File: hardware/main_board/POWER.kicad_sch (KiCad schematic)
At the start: 1 part, among them J1 USB_C_Receptacle_PowerOnly_6P

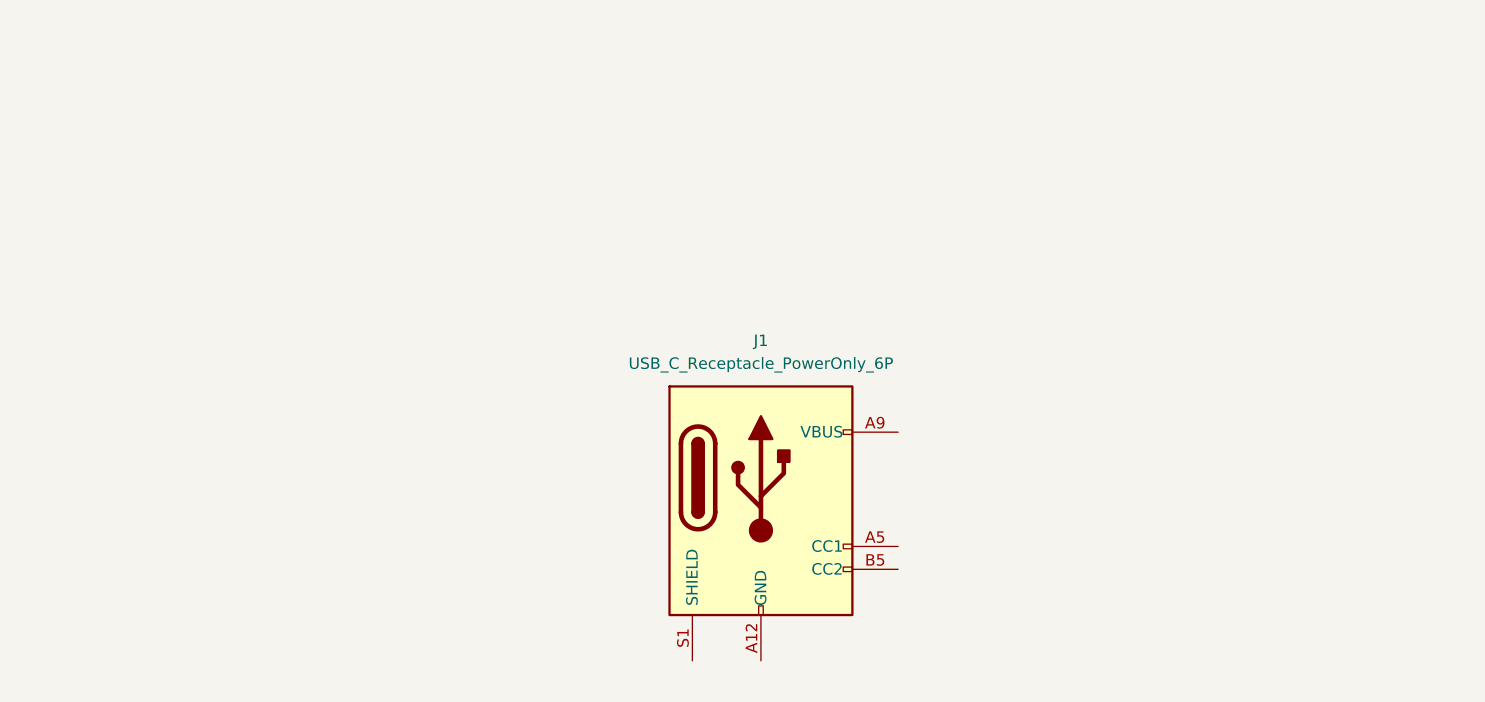
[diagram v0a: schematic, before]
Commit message: fixed sides of peripheral board not being symmetrical. added teardrops. name of board tbd
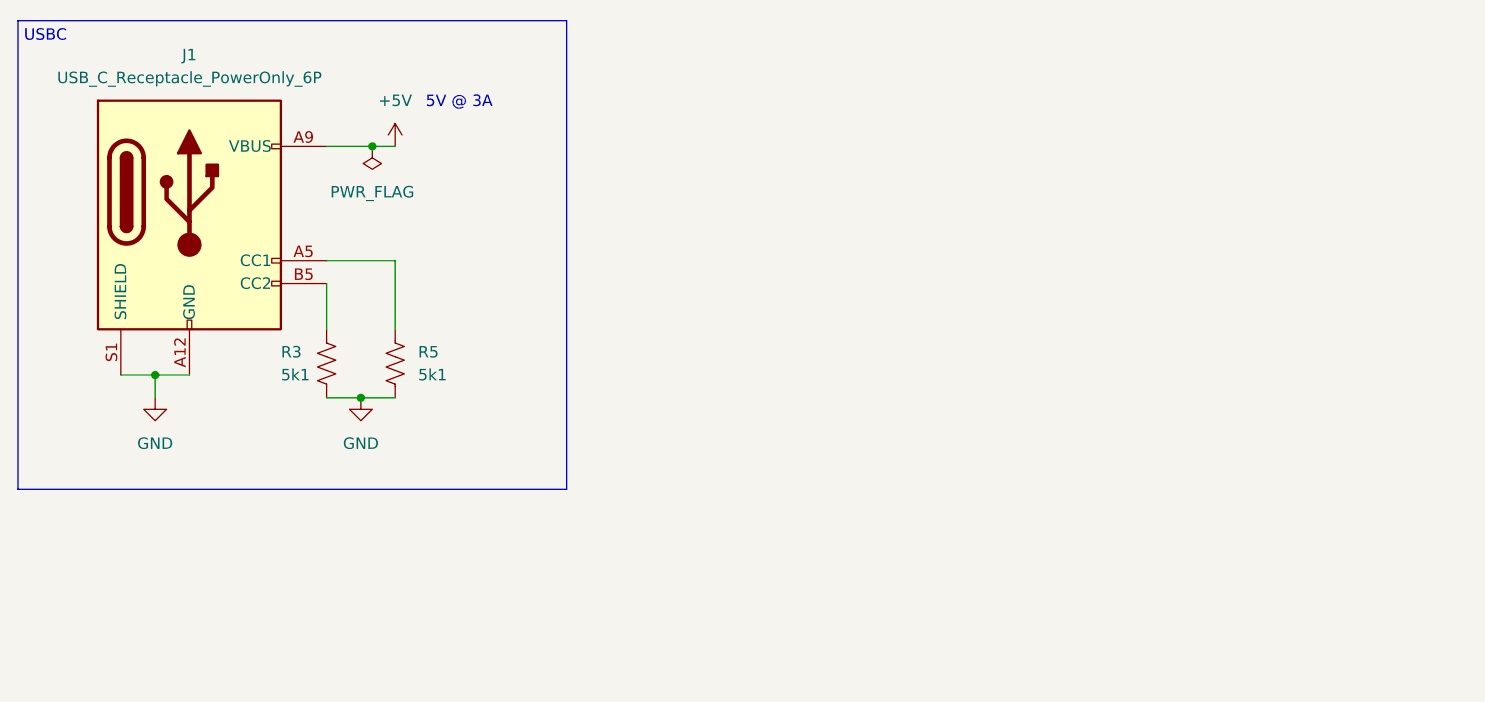
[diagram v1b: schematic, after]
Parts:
- added R3, R5: 5k1, symbol Device:R_US
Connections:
- net GND: now reaches J1.A12 (GND), J1.B12 (GND)
- net GND: now also J1.S1 (SHIELD), R3.2, R5.2
- net at J1.A5 (CC1): now also R5.1
- net +5V: now reaches J1.A9 (VBUS), J1.B9 (VBUS)
- net at J1.B5 (CC2): now also R3.1
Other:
- note added: "5V @ 3A"
- note added: "USBC"
- moved on the sheet: J1

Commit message: drew schematic
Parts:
- removed J1: USB_C_Receptacle_PowerOnly_6P, symbol Connector:USB_C_Receptacle_PowerOnly_6P
- added C10, C11, C9: 10u, Capacitor_SMD:C_0805_2012Metric, symbol Device:C
- added C12: u1, Capacitor_SMD:C_0805_2012Metric, symbol Device:C
- added IC4: TPS63000IDRCRQ1, SamacSys_Parts:TPS63000IDRCRQ1, symbol SamacSys_Parts:TPS63000IDRCRQ1
- added J6: UJC-H-G-SMT-1-P6-TR, SamacSys_Parts:UJCHGSMT1P6TR, symbol Connector:USB_C_Receptacle_PowerOnly_6P
- added L1: 2u2, SamacSys_Parts:NRS3015T2R2MNGHV, symbol Device:L
- added NT2: NetTie, SamacSys_Parts:NetTie-2_Pad0.3mm, symbol SamacSys_Parts:NetTie
- added R10: 100, Resistor_SMD:R_0805_2012Metric, symbol Device:R_US
- added R11: 1M, Resistor_SMD:R_0805_2012Metric, symbol Device:R_US
- added R14: 200k, Resistor_SMD:R_0805_2012Metric, symbol Device:R_US
- R12: renamed from R3; footprint (none) -> Resistor_SMD:R_0805_2012Metric
- R13: renamed from R5; footprint (none) -> Resistor_SMD:R_0805_2012Metric
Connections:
- net +5V: now also J6.A9 (VBUS), J6.B9 (VBUS)
- net GND: now also C12.2, IC4.9 (GND), J6.A12 (GND), J6.B12 (GND), J6.S1 (SHIELD), NT2.1, R14.2
- net at R13.1: now also J6.A5 (CC1)
- net at R12.1: now also J6.B5 (CC2)
- new net: IC4.10 (FB), R11.2, R14.1
- new net: C12.1, IC4.6 (EN), IC4.7 (PS/SYNC), IC4.8 (VINA), R10.2
- new net: IC4.4 (L1), L1.1
- new net: IC4.2 (L2), L1.2
- new net +3V3: C10.1, C11.1, IC4.1 (VOUT), R11.1
- new net BUCK_VIN: C9.1, IC4.5 (VIN), R10.1
- new net GNDPWR: C10.2, C11.2, C9.2, IC4.11 (PGND_2), IC4.12 (PGND_3), IC4.13 (PGND_4), IC4.14 (PGND_5), IC4.15 (PGND_6), IC4.3 (PGND_1), NT2.2
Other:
- note added: "Buck Converter (5V to 3V3)"
- moved on the sheet: R12, R13

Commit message: save before nuke SPI ADC
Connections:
- net BUCK_VIN is gone; now on net +5V: C9.1, IC4.5 (VIN), R10.1
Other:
- moved on the sheet: R10
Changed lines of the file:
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@@
+	)
+	(junction
+		(at 85.09 38.1)
+		(diameter 0)
+		(color 0 0 0 0)
 	)
 	(junction
@@
 	)
 	(junction
+		(at 160.02 41.91)
+		(diameter 0)
+		(color 0 0 0 0)
+	)
+	(junction
 		(at 130.81 73.66)
 		(diameter 0)
@@
 	(wire
 		(pts
+			(xy 160.02 41.91) (xy 165.1 41.91)
+		)
+		(stroke
+			(width 0)
+			(type default)
+		)
+	)
+	(wire
+		(pts
 			(xy 165.1 41.91) (xy 170.18 41.91)
 		)
@@
 	(wire
 		(pts
+			(xy 97.79 39.37) (xy 97.79 38.1)
+		)
+		(stroke
+			(width 0)
+			(type default)
+		)
+	)
+	(wire
+		(pts
 			(xy 120.65 22.86) (xy 106.68 22.86)
 		)
@@
 	(wire
 		(pts
-			(xy 157.48 41.91) (xy 165.1 41.91)
+			(xy 157.48 41.91) (xy 160.02 41.91)
 		)
 		(stroke
@@
 			(width 0)
 			(type default)
-		)
-	)
-	(wire
-		(pts
-			(xy 97.79 45.72) (xy 97.79 46.99)
-		)
-		(stroke
-			(width 0)
-			(type default)
-		)
-	)
-	(label "BUCK_VIN"
-		(at 87.63 38.1 0)
-		(effects
-			(font
-				(size 1.27 1.27)
-			)
-			(justify left bottom)
 		)
 	)
@@
 	(symbol
 		(lib_id "Device:R_US")
-		(at 97.79 41.91 0)
+		(at 97.79 43.18 0)
 		(unit 1)
 		(exclude_from_sim no)
@@
 		(fields_autoplaced yes)
 		(property "Reference" "R10"
-			(at 100.33 40.6399 0)
+			(at 100.33 41.9099 0)
 			(effects
 				(font
@@
 		)
 		(property "Value" "100"
-			(at 100.33 43.1799 0)
+			(at 100.33 44.4499 0)
 			(effects
 				(font
@@
 		)
 		(property "Footprint" "Resistor_SMD:R_0805_2012Metric"
-			(at 111.76 138.1 0)
+			(at 111.76 139.37 0)
 			(effects
 				(font
@@
 		)
 		(property "Datasheet" "https://componentsearchengine.com//ESR03EZPF1000.pdf"
-			(at 111.76 238.1 0)
+			(at 111.76 239.37 0)
 			(effects
 				(font
@@
 		)
 		(property "Description" "Thick Film Resistors - SMD 0603 100ohm 1% Anti Surge AEC-Q200"
-			(at 97.79 41.91 0)
+			(at 97.79 43.18 0)
 			(effects
 				(font
@@
 		)
 		(property "Height" "0.55"
-			(at 111.76 438.1 0)
+			(at 111.76 439.37 0)
 			(effects
 				(font
@@
 		)
 		(property "Mouser Part Number" "755-ESR03EZPF1000"
-			(at 111.76 538.1 0)
+			(at 111.76 539.37 0)
 			(effects
 				(font
@@
 		)
 		(property "Mouser Price/Stock" "https://www.mouser.co.uk/ProductDetail/ROHM-Semiconductor/ESR03EZPF1000?qs=493kPxzlxfJdLkJZpX4ByA%3D%3D"
-			(at 111.76 638.1 0)
+			(at 111.76 639.37 0)
 			(effects
 				(font
@@
 		)
 		(property "Manufacturer_Name" "ROHM Semiconductor"
-			(at 111.76 738.1 0)
+			(at 111.76 739.37 0)
 			(effects
 				(font
@@
 		)
 		(property "Manufacturer_Part_Number" "ESR03EZPF1000"
-			(at 111.76 838.1 0)
+			(at 111.76 839.37 0)
 			(effects
 				(font
@@
 	(symbol
 		(lib_id "power:PWR_FLAG")
+		(at 160.02 41.91 0)
+		(unit 1)
+		(exclude_from_sim no)
+		(in_bom yes)
+		(on_board yes)
+		(dnp no)
+		(fields_autoplaced yes)
+		(property "Reference" "#FLG04"
+			(at 160.02 40.005 0)
+			(effects
+				(font
+					(size 1.27 1.27)
+				)
+				(hide yes)
+			)
+		)
+		(property "Value" "PWR_FLAG"
+			(at 160.02 36.83 0)
+			(effects
+				(font
+					(size 1.27 1.27)
+				)
+			)
+		)
+		(property "Footprint" ""
+			(at 160.02 41.91 0)
+			(effects
+				(font
+					(size 1.27 1.27)
+				)
+				(hide yes)
+			)
+		)
+		(property "Datasheet" "~"
+			(at 160.02 41.91 0)
+			(effects
+				(font
+					(size 1.27 1.27)
+				)
+				(hide yes)
+			)
+		)
+		(property "Description" "Special symbol for telling ERC where power comes from"
+			(at 160.02 41.91 0)
+			(effects
+				(font
+					(size 1.27 1.27)
+				)
+				(hide yes)
+			)
+		)
+		(pin "1"
+		)
+		(instances
+			(project ""
+				(path "/5332464e-0c3a-49d2-8fb5-731d0e42ee15/699e22c4-7494-4d98-a0c1-55c97e2e9226"
+					(reference "#FLG04")
+					(unit 1)
+				)
+			)
+		)
+	)
+	(symbol
+		(lib_id "power:PWR_FLAG")
 		(at 167.64 60.96 0)
 		(unit 1)
@@
 					(unit 1)
 				)
+			)
+		)
+	)
+	(symbol
+		(lib_id "power:+5V")
+		(at 85.09 38.1 0)
+		(unit 1)
+		(exclude_from_sim no)
+		(in_bom yes)
+		(on_board yes)
+		(dnp no)
+		(fields_autoplaced yes)
+		(property "Reference" "#PWR067"
+			(at 85.09 41.91 0)
+			(effects
+				(font
+					(size 1.27 1.27)
+				)
+				(hide yes)
+			)
+		)
+		(property "Value" "+5V"
+			(at 85.09 33.02 0)
+			(effects
+				(font
+					(size 1.27 1.27)
+				)
+			)
+		)
+		(property "Footprint" ""
+			(at 85.09 38.1 0)
+			(effects
+				(font
+					(size 1.27 1.27)
+				)
+				(hide yes)
+			)
+		)
+		(property "Datasheet" ""
+			(at 85.09 38.1 0)
+			(effects
+				(font
+					(size 1.27 1.27)
+				)
+				(hide yes)
+			)
+		)
+		(property "Description" "Power symbol creates a global label with name \"+5V\""
+			(at 85.09 38.1 0)
+			(effects
+				(font
+					(size 1.27 1.27)
+				)
+				(hide yes)
+			)
+		)
+		(pin "1"
+		)
+		(instances
+			(project "main_board"
+				(path "/5332464e-0c3a-49d2-8fb5-731d0e42ee15/699e22c4-7494-4d98-a0c1-55c97e2e9226"
+					(reference "#PWR067")
+					(unit 1)
+				)
